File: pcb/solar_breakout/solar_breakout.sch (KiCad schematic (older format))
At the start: 15 parts

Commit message: Work on solar breakout board
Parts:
- removed D?: D, symbol agg-kicad:D
- removed R?: 5.1k, symbol agg-kicad:R
- added C?: 22p, symbol agg-kicad:C
- added C?: 1u, symbol agg-kicad:C
- added D?: MRA4003T3, agg:DO-214AC-SMA, symbol agg-kicad:D
- added J? (x4): CONN_01x02, agg:SIL-254P-02, symbol agg-kicad:CONN_01x02
- added R?: 3.3, agg:2512, symbol agg-kicad:R
- added R?: R, symbol agg-kicad:R
- added SC? (x3): Solar_Cell, symbol solar_cell:Solar_Cell
- added U? (x2): SM74611, solar_breakout:SM74611, symbol sm74611:SM74611
- added X?: Jumper, symbol agg-kicad:PART
- C?: footprint (none) -> agg:0402; Farnell (none) -> 2495145
- D?: value D -> MRA4003T3; footprint (none) -> agg:DO-214AC-SMA; Farnell (none) -> 1459134
- J? (x2): footprint (none) -> agg:SIL-254P-02; Farnell (none) -> 1593458
- L?: value 6.8u -> 10u; Farnell (none) -> Value
- SC?: symbol Device:Solar_Cell -> solar_cell:Solar_Cell; Digikey (none) -> Value; Farnell (none) -> Value
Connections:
- net Cap_V: now also C?.2, IC?.9 (VOUT), R?.1, C?.1, C?.2, J?.2
- net GND: now also C?.2, D?.1, J?.2, J?.2, J?.2, R?.2, SC?.2 (-), SC?.2 (-)
- net at IC?.1 (FB), R?.1, R?.2: now also C?.1
- net at IC?.5 (MPPC): now also R?.1
- net D_anode: now reaches C?.1, D?.2
- net D_anode: now also J?.1, R?.2
- net at D?.1: now also D?.2
- net Array_1_+: now reaches SC?.1 (+)
- net Array_1_+: now also J?.1, U?.1 (Anode)
- net at SC?.2 (-): now also SC?.1 (+)
- new net: SC?.1 (+), SC?.2 (-)
- new net: U?.DAP (Cathode), U?.DAP (Cathode)
- new net: J?.1, R?.1
- new net Array_2_+: J?.1, SC?.1 (+), U?.1 (Anode)
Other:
- note added: "1V"
- note added: "Board to board connectors"
- note added: "Change value to set max power point \n(use ltspice and IV curves for solar panels)"
- note added: "Discharge jumper (short to discharge capacitor)\nREMOVE BEFORE FLIGHT"
- note added: "Flying wires, \nthermally coupled\nto solar cells\n(no smd footprint)"
- note added: "Holes for flying wires"
- note added: "Low DCR"
- note added: "Low ESR"
- note added: "Low ESR\nClose to converter pins"
- note added: "Off board components"
- note added: "Tabbing wire"
- note added: "Thermally coupled to solar cells"
- moved on the sheet: C?, D?, IC?, J?, L?, R?, SC?

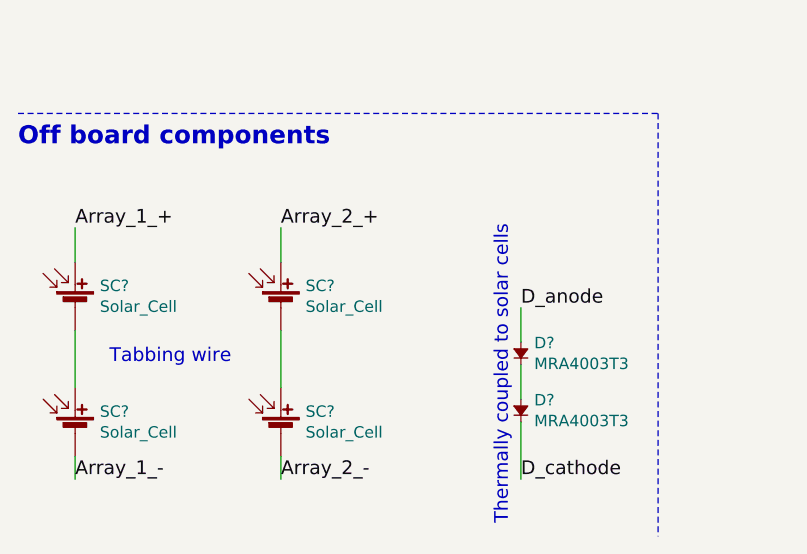
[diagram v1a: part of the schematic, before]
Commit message: Add wspr breakout board and reorganise sub project libraries
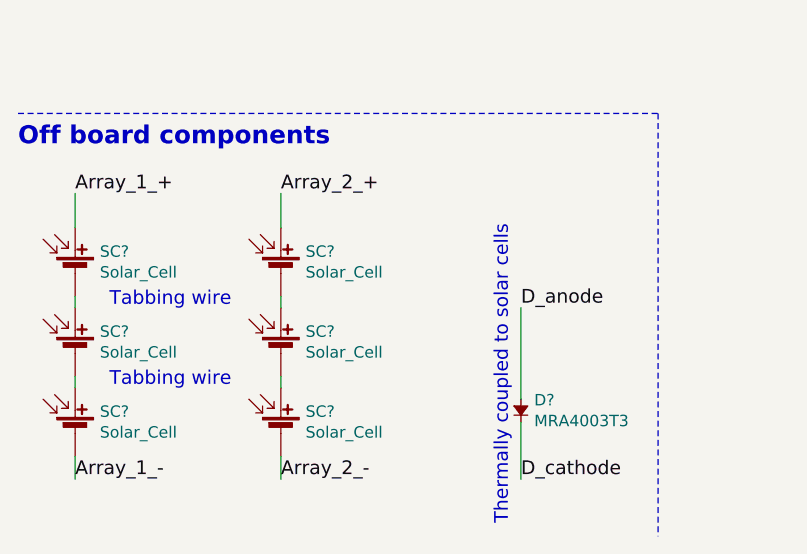
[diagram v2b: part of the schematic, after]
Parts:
- removed D?: MRA4003T3, agg:DO-214AC-SMA, symbol agg-kicad:D
- added SC? (x2): Solar_Cell, symbol solar_cell:Solar_Cell
- J? (x3): Farnell 1593458 -> 1593411
- J? (x2): Farnell Value -> (none)
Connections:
- net D_anode: now also D?.2
- net at SC?.2 (-): now also SC?.1 (+); no longer SC?.1 (+)
- net at SC?.1 (+): now also SC?.2 (-); no longer SC?.2 (-)
- new net: SC?.1 (+), SC?.2 (-) (x2)
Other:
- moved on the sheet: SC?
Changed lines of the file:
@@
 F 2 "agg:SIL-254P-02" H 6000 1900 50  0001 C CNN
 F 3 "" H 6000 1900 50  0001 C CNN
-F 4 "1593458" H 6000 1900 60  0001 C CNN "Farnell"
+F 4 "1593411" H 6000 1900 60  0001 C CNN "Farnell"
 	1    6000 1900
 	1    0    0    -1
@@
 F 2 "agg:SIL-254P-02" H 7250 1900 50  0001 C CNN
 F 3 "" H 7250 1900 50  0001 C CNN
-F 4 "1593458" H 7250 1900 60  0001 C CNN "Farnell"
+F 4 "1593411" H 7250 1900 60  0001 C CNN "Farnell"
 	1    7250 1900
 	1    0    0    -1
@@
 $EndComp
 $Comp
-L agg-kicad:D D?
-U 1 1 5A7CBF10
-P 2700 7000
-F 0 "D?" V 2796 6942 50  0000 R CNN
-F 1 "MRA4003T3" V 2705 6942 50  0000 R CNN
-F 2 "agg:DO-214AC-SMA" H 2700 7000 50  0001 C CNN
-F 3 "http://www.farnell.com/datasheets/2028669.pdf" H 2700 7000 50  0001 C CNN
-F 4 "1459134" H 2700 7000 60  0001 C CNN "Farnell"
-	1    2700 7000
-	0    -1   -1   0
-$EndComp
-$Comp
 L agg-kicad:GND #PWR?
 U 1 1 5A7CCCAD
@@
 L solar_cell:Solar_Cell SC?
 U 1 1 5A7F06D9
-P 750 6750
-F 0 "SC?" H 858 6846 50  0000 L CNN
-F 1 "Solar_Cell" H 858 6755 50  0000 L CNN
-F 2 "" V 750 6810 50  0001 C CNN
-F 3 "~" V 750 6810 50  0001 C CNN
-F 4 "Value" H 750 6750 60  0001 C CNN "Digikey"
-F 5 "Value" H 750 6750 60  0001 C CNN "Farnell"
-	1    750  6750
+P 750 6600
+F 0 "SC?" H 858 6696 50  0000 L CNN
+F 1 "Solar_Cell" H 858 6605 50  0000 L CNN
+F 2 "" V 750 6660 50  0001 C CNN
+F 3 "~" V 750 6660 50  0001 C CNN
+F 4 "Value" H 750 6600 60  0001 C CNN "Digikey"
+F 5 "Value" H 750 6600 60  0001 C CNN "Farnell"
+	1    750  6600
 	1    0    0    -1
 $EndComp
@@
 L solar_cell:Solar_Cell SC?
 U 1 1 5A7CDA84
-P 1650 6750
-F 0 "SC?" H 1758 6846 50  0000 L CNN
-F 1 "Solar_Cell" H 1758 6755 50  0000 L CNN
-F 2 "" V 1650 6810 50  0001 C CNN
-F 3 "~" V 1650 6810 50  0001 C CNN
-F 4 "Value" H 1650 6750 60  0001 C CNN "Digikey"
-F 5 "Value" H 1650 6750 60  0001 C CNN "Farnell"
-	1    1650 6750
+P 1650 6600
+F 0 "SC?" H 1758 6696 50  0000 L CNN
+F 1 "Solar_Cell" H 1758 6605 50  0000 L CNN
+F 2 "" V 1650 6660 50  0001 C CNN
+F 3 "~" V 1650 6660 50  0001 C CNN
+F 4 "Value" H 1650 6600 60  0001 C CNN "Digikey"
+F 5 "Value" H 1650 6600 60  0001 C CNN "Farnell"
+	1    1650 6600
 	1    0    0    -1
 $EndComp
@@
 	6250 3450 6250 3500
 Connection ~ 6250 3500
-Wire Wire Line
-	750  7100 750  6850
-Wire Wire Line
-	1650 7100 1650 6850
 $Comp
 L agg-kicad:C C?
@@
 Wire Wire Line
 	750  7500 750  7400
-Text Notes 900  7000 0    60   ~ 0
+Text Notes 900  7100 0    60   ~ 0
 Tabbing wire
 Text Notes 900  1750 0    60   ~ 0
@@
 F 1 "LTC3105" H 5800 3934 50  0000 C CNN
 F 2 "agg:DFN-10-EP-LT" H 5500 2900 50  0001 L CNN
-F 3 "" H 5400 3800 50  0001 C CNN
+F 3 "http://www.farnell.com/datasheets/1999327.pdf" H 5400 3800 50  0001 C CNN
 F 4 "1898600" H 5500 2800 50  0001 L CNN "Farnell"
 	1    5800 3500
@@
 $EndComp
 Wire Wire Line
-	2700 7150 2700 7000
+	2700 6750 2700 7150
 $Comp
 L agg-kicad:CONN_01x02 J?
@@
 F 2 "agg:SIL-254P-02" H 1950 1650 50  0001 C CNN
 F 3 "" H 1950 1650 50  0001 C CNN
-F 4 "Value" H 1950 1650 60  0001 C CNN "Farnell"
 	1    1950 1650
 	1    0    0    -1
@@
 F 2 "agg:SIL-254P-02" H 1950 3150 50  0001 C CNN
 F 3 "" H 1950 3150 50  0001 C CNN
-F 4 "Value" H 1950 3150 60  0001 C CNN "Farnell"
 	1    1950 3150
 	1    0    0    -1
@@
 F 2 "agg:SIL-254P-02" H 7550 3500 50  0001 C CNN
 F 3 "" H 7550 3500 50  0001 C CNN
-F 4 "1593458" H 7550 3500 60  0001 C CNN "Farnell"
+F 4 "1593411" H 7550 3500 60  0001 C CNN "Farnell"
 	1    7550 3500
 	-1   0    0    1
@@
 	1    0    0    -1
 $EndComp
-Text Label 750  6400 0    60   ~ 0
+Text Label 750  6250 0    60   ~ 0
 Array_1_+
-Text Label 1650 6400 0    60   ~ 0
+Text Label 1650 6250 0    60   ~ 0
 Array_2_+
 Text Label 2700 6750 0    60   ~ 0
 D_anode
 Wire Wire Line
-	2700 6900 2700 6750
-Wire Wire Line
-	750  6550 750  6400
-Wire Wire Line
-	1650 6550 1650 6400
+	750  6400 750  6250
+Wire Wire Line
+	1650 6400 1650 6250
 $Comp
 L agg-kicad:CONN_01x02 J?
@@
 Text Notes 500  6050 0    79   ~ 16
 Off board components
-Text Notes 2650 7700 1    60   ~ 0
-Thermally coupled to solar cells
 Text Notes 850  3250 0    60   ~ 0
 Holes for flying wires
@@
 Text Notes 4900 3500 0    20   ~ 0
 Change value to set max power point \n(use ltspice and IV curves for solar panels)
+$Comp
+L solar_cell:Solar_Cell SC?
+U 1 1 5A89D9A5
+P 750 6950
+F 0 "SC?" H 858 7046 50  0000 L CNN
+F 1 "Solar_Cell" H 858 6955 50  0000 L CNN
+F 2 "" V 750 7010 50  0001 C CNN
+F 3 "~" V 750 7010 50  0001 C CNN
+F 4 "Value" H 750 6950 60  0001 C CNN "Digikey"
+F 5 "Value" H 750 6950 60  0001 C CNN "Farnell"
+	1    750  6950
+	1    0    0    -1
+$EndComp
+$Comp
+L solar_cell:Solar_Cell SC?
+U 1 1 5A89D9F9
+P 1650 6950
+F 0 "SC?" H 1758 7046 50  0000 L CNN
+F 1 "Solar_Cell" H 1758 6955 50  0000 L CNN
+F 2 "" V 1650 7010 50  0001 C CNN
+F 3 "~" V 1650 7010 50  0001 C CNN
+F 4 "Value" H 1650 6950 60  0001 C CNN "Digikey"
+F 5 "Value" H 1650 6950 60  0001 C CNN "Farnell"
+	1    1650 6950
+	1    0    0    -1
+$EndComp
+Text Notes 900  6750 0    60   ~ 0
+Tabbing wire
+Wire Wire Line
+	1650 6700 1650 6750
+Wire Wire Line
+	1650 7050 1650 7100
+Wire Wire Line
+	750  7100 750  7050
+Wire Wire Line
+	750  6750 750  6700
+Text Notes 2650 7700 1    60   ~ 0
+Thermally coupled to solar cells
 $EndSCHEMATC

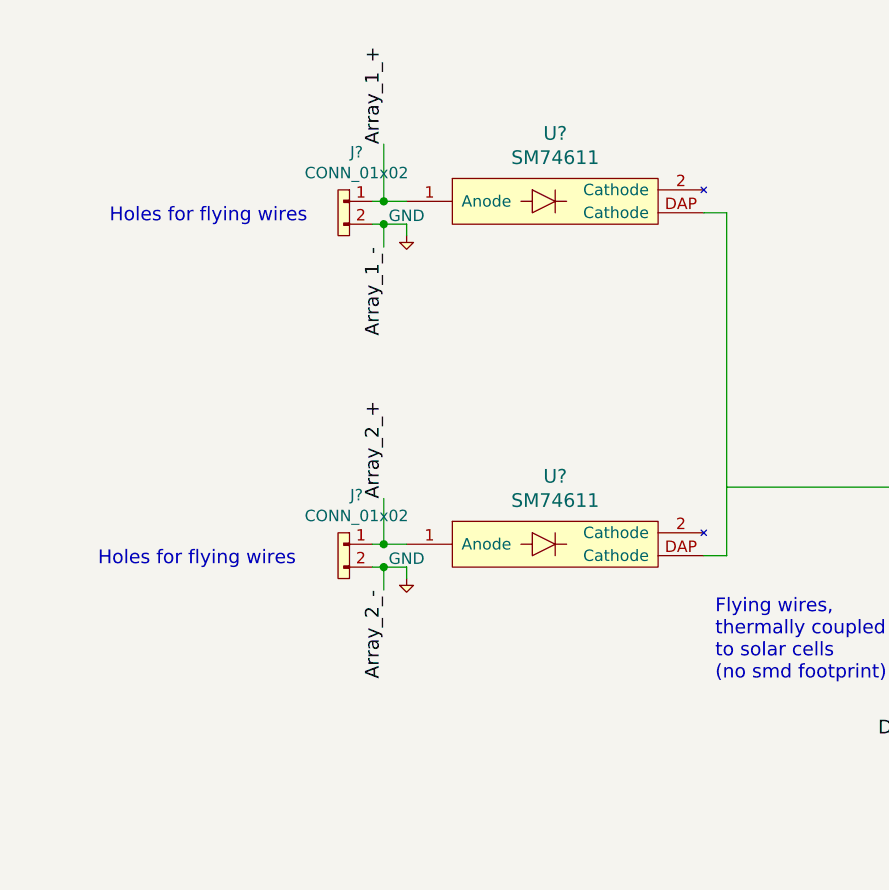
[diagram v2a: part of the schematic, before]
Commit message: Use schottky diode in solar breakout, compensate with extra series solar panels
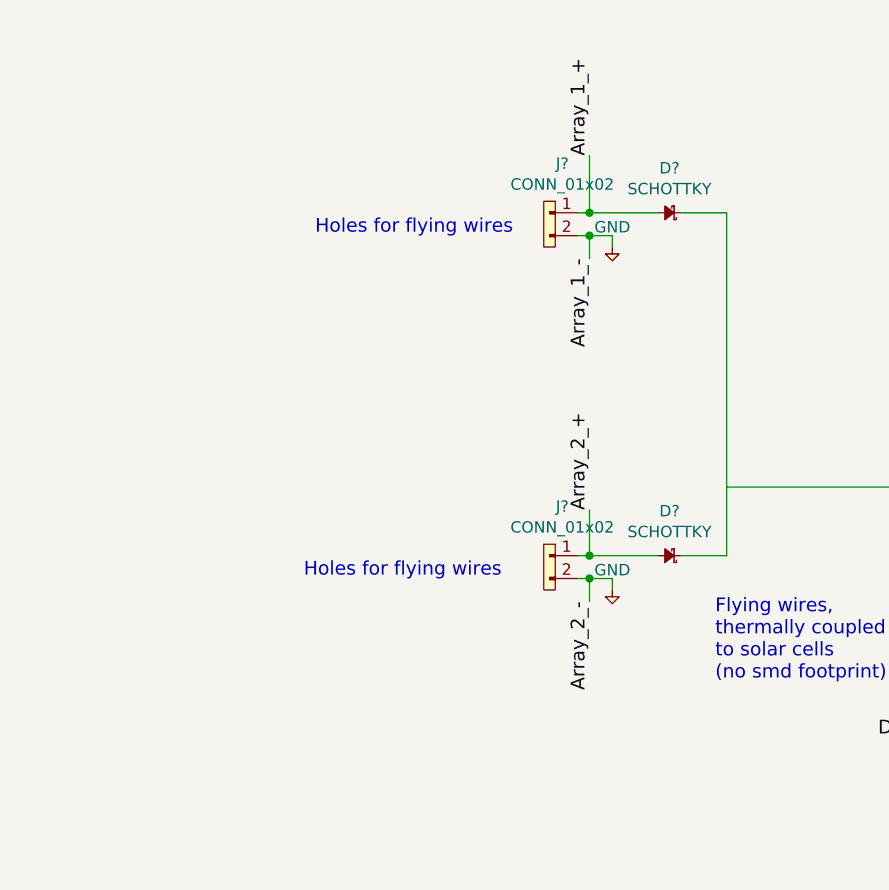
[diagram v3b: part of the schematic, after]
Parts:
- removed U? (x2): SM74611, solar_breakout:SM74611, symbol sm74611:SM74611
- added D? (x2): SCHOTTKY, jerboa:SMA_DIODE, symbol agg-kicad:SCHOTTKY
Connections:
- net Array_1_+: now also D?.2
- net Array_2_+: now also D?.2
- new net: D?.1, D?.1
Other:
- moved on the sheet: J?
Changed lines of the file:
@@
 Text Notes 5350 2850 0    60   ~ 0
 1V
-$Comp
-L sm74611:SM74611 U?
-U 1 1 5A7DE91F
-P 2850 1650
-F 0 "U?" H 2850 1947 60  0000 C CNN
-F 1 "SM74611" H 2850 1841 60  0000 C CNN
-F 2 "solar_breakout:SM74611" H 2200 1700 60  0001 C CNN
-F 3 "http://www.ti.com/lit/ds/symlink/sm74611.pdf" H 2850 1400 60  0001 C CNN
-F 4 "2492333" H 2850 1300 60  0001 C CNN "Farnell"
-	1    2850 1650
-	1    0    0    -1
-$EndComp
-$Comp
-L sm74611:SM74611 U?
-U 1 1 5A7DEA61
-P 2850 3150
-F 0 "U?" H 2850 3447 60  0000 C CNN
-F 1 "SM74611" H 2850 3341 60  0000 C CNN
-F 2 "solar_breakout:SM74611" H 2200 3200 60  0001 C CNN
-F 3 "http://www.ti.com/lit/ds/symlink/sm74611.pdf" H 2850 2900 60  0001 C CNN
-F 4 "2492333" H 2850 2800 60  0001 C CNN "Farnell"
-	1    2850 3150
-	1    0    0    -1
-$EndComp
 Wire Wire Line
 	1650 7500 1650 7400
@@
 Text Notes 900  7100 0    60   ~ 0
 Tabbing wire
-Text Notes 900  1750 0    60   ~ 0
+Text Notes 1800 1800 0    60   ~ 0
 Holes for flying wires
 Text Label 7600 3300 0    50   ~ 0
@@
 L agg-kicad:CONN_01x02 J?
 U 1 1 5A7F3534
-P 1950 1650
-F 0 "J?" H 1981 1865 50  0000 C CNN
-F 1 "CONN_01x02" H 1981 1774 50  0000 C CNN
-F 2 "agg:SIL-254P-02" H 1950 1650 50  0001 C CNN
-F 3 "" H 1950 1650 50  0001 C CNN
-	1    1950 1650
+P 2850 1700
+F 0 "J?" H 2881 1915 50  0000 C CNN
+F 1 "CONN_01x02" H 2881 1824 50  0000 C CNN
+F 2 "agg:SIL-254P-02" H 2850 1700 50  0001 C CNN
+F 3 "" H 2850 1700 50  0001 C CNN
+	1    2850 1700
 	1    0    0    -1
 $EndComp
@@
 L agg-kicad:CONN_01x02 J?
 U 1 1 5A7F3705
-P 1950 3150
-F 0 "J?" H 1981 3365 50  0000 C CNN
-F 1 "CONN_01x02" H 1981 3274 50  0000 C CNN
-F 2 "agg:SIL-254P-02" H 1950 3150 50  0001 C CNN
-F 3 "" H 1950 3150 50  0001 C CNN
-	1    1950 3150
+P 2850 3200
+F 0 "J?" H 2881 3415 50  0000 C CNN
+F 1 "CONN_01x02" H 2881 3324 50  0000 C CNN
+F 2 "agg:SIL-254P-02" H 2850 3200 50  0001 C CNN
+F 3 "" H 2850 3200 50  0001 C CNN
+	1    2850 3200
 	1    0    0    -1
 $EndComp
@@
 L agg-kicad:GND #PWR?
 U 1 1 5A7F37F7
-P 2200 3300
-F 0 "#PWR?" H 2070 3340 50  0001 L CNN
-F 1 "GND" H 2200 3387 50  0000 C CNN
-F 2 "" H 2200 3300 50  0001 C CNN
-F 3 "" H 2200 3300 50  0001 C CNN
-	1    2200 3300
+P 3100 3350
+F 0 "#PWR?" H 2970 3390 50  0001 L CNN
+F 1 "GND" H 3100 3437 50  0000 C CNN
+F 2 "" H 3100 3350 50  0001 C CNN
+F 3 "" H 3100 3350 50  0001 C CNN
+	1    3100 3350
 	1    0    0    -1
 $EndComp
@@
 L agg-kicad:GND #PWR?
 U 1 1 5A7F385E
-P 2200 1800
-F 0 "#PWR?" H 2070 1840 50  0001 L CNN
-F 1 "GND" H 2200 1887 50  0000 C CNN
-F 2 "" H 2200 1800 50  0001 C CNN
-F 3 "" H 2200 1800 50  0001 C CNN
-	1    2200 1800
-	1    0    0    -1
-$EndComp
-Wire Wire Line
-	2050 3250 2200 3250
-Wire Wire Line
-	2200 3250 2200 3300
-Wire Wire Line
-	2200 3150 2050 3150
-Wire Wire Line
-	2050 1650 2200 1650
-Wire Wire Line
-	2050 1750 2200 1750
-Wire Wire Line
-	2200 1750 2200 1800
+P 3100 1850
+F 0 "#PWR?" H 2970 1890 50  0001 L CNN
+F 1 "GND" H 3100 1937 50  0000 C CNN
+F 2 "" H 3100 1850 50  0001 C CNN
+F 3 "" H 3100 1850 50  0001 C CNN
+	1    3100 1850
+	1    0    0    -1
+$EndComp
+Wire Wire Line
+	2950 3300 3100 3300
+Wire Wire Line
+	3100 3300 3100 3350
+Wire Wire Line
+	2950 3200 3300 3200
+Wire Wire Line
+	2950 1700 3300 1700
+Wire Wire Line
+	2950 1800 3100 1800
+Wire Wire Line
+	3100 1800 3100 1850
 Text Notes 7750 3500 0    60   ~ 0
 Discharge jumper (short to discharge capacitor)\nREMOVE BEFORE FLIGHT
@@
 Wire Wire Line
 	2700 7500 2700 7250
-Text Label 2100 1400 1    60   ~ 0
+Text Label 3000 1450 1    60   ~ 0
 Array_1_+
-Text Label 2100 2950 1    60   ~ 0
+Text Label 3000 3000 1    60   ~ 0
 Array_2_+
-Text Label 2100 1850 3    60   ~ 0
+Text Label 3000 1900 3    60   ~ 0
 Array_1_-
-Text Label 2100 3350 3    60   ~ 0
+Text Label 3000 3400 3    60   ~ 0
 Array_2_-
 Wire Wire Line
-	2100 3350 2100 3250
-Connection ~ 2100 3250
-Wire Wire Line
-	2100 2950 2100 3150
-Connection ~ 2100 3150
-Wire Wire Line
-	2100 1850 2100 1750
-Connection ~ 2100 1750
-Wire Wire Line
-	2100 1400 2100 1650
-Connection ~ 2100 1650
+	3000 3400 3000 3300
+Connection ~ 3000 3300
+Wire Wire Line
+	3000 3000 3000 3200
+Connection ~ 3000 3200
+Wire Wire Line
+	3000 1900 3000 1800
+Connection ~ 3000 1800
+Wire Wire Line
+	3000 1450 3000 1700
+Connection ~ 3000 1700
 Text Label 4700 3300 2    60   ~ 0
 D_anode
@@
 Text Notes 500  6050 0    79   ~ 16
 Off board components
-Text Notes 850  3250 0    60   ~ 0
+Text Notes 1750 3300 0    60   ~ 0
 Holes for flying wires
 Text Notes 6150 2200 0    60   ~ 0
 Board to board connectors
 Wire Wire Line
-	3500 3200 3600 3200
+	3400 3200 3600 3200
 Wire Wire Line
 	3600 1700 3600 3200
 Wire Wire Line
-	3600 1700 3500 1700
+	3400 1700 3600 1700
 $Comp
 L agg-kicad:R R?
@@
 Text Notes 2650 7700 1    60   ~ 0
 Thermally coupled to solar cells
+$Comp
+L agg-kicad:SCHOTTKY D?
+U 1 1 5A89E92B
+P 3400 1700
+F 0 "D?" H 3450 1505 50  0000 C CNN
+F 1 "SCHOTTKY" H 3450 1596 50  0000 C CNN
+F 2 "jerboa:SMA_DIODE" H 3350 1670 50  0001 C CNN
+F 3 "http://www.farnell.com/datasheets/2238474.pdf" H 3450 1770 50  0001 C CNN
+F 4 "1843668" H 3400 1700 60  0001 C CNN "Farnell"
+	1    3400 1700
+	-1   0    0    1
+$EndComp
+$Comp
+L agg-kicad:SCHOTTKY D?
+U 1 1 5A8AD345
+P 3400 3200
+F 0 "D?" H 3450 3005 50  0000 C CNN
+F 1 "SCHOTTKY" H 3450 3096 50  0000 C CNN
+F 2 "jerboa:SMA_DIODE" H 3350 3170 50  0001 C CNN
+F 3 "http://www.farnell.com/datasheets/2238474.pdf" H 3450 3270 50  0001 C CNN
+F 4 "1843668" H 3400 3200 60  0001 C CNN "Farnell"
+	1    3400 3200
+	-1   0    0    1
+$EndComp
 $EndSCHEMATC
